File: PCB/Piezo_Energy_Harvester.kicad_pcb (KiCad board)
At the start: 2 copper layers, 26 x 20 mm, 9 parts, among them J1 Conn_01x01_Pin, J2 Conn_01x01_Pin, U1 LTC3588IMSE-1-PBF

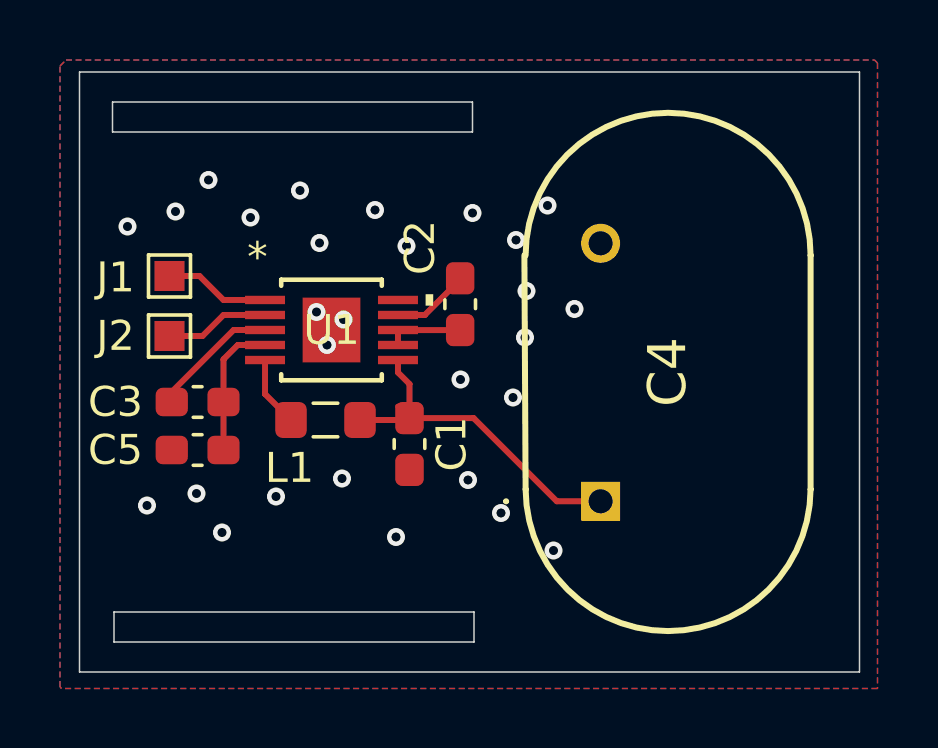
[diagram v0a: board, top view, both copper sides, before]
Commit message: changed coil footprint
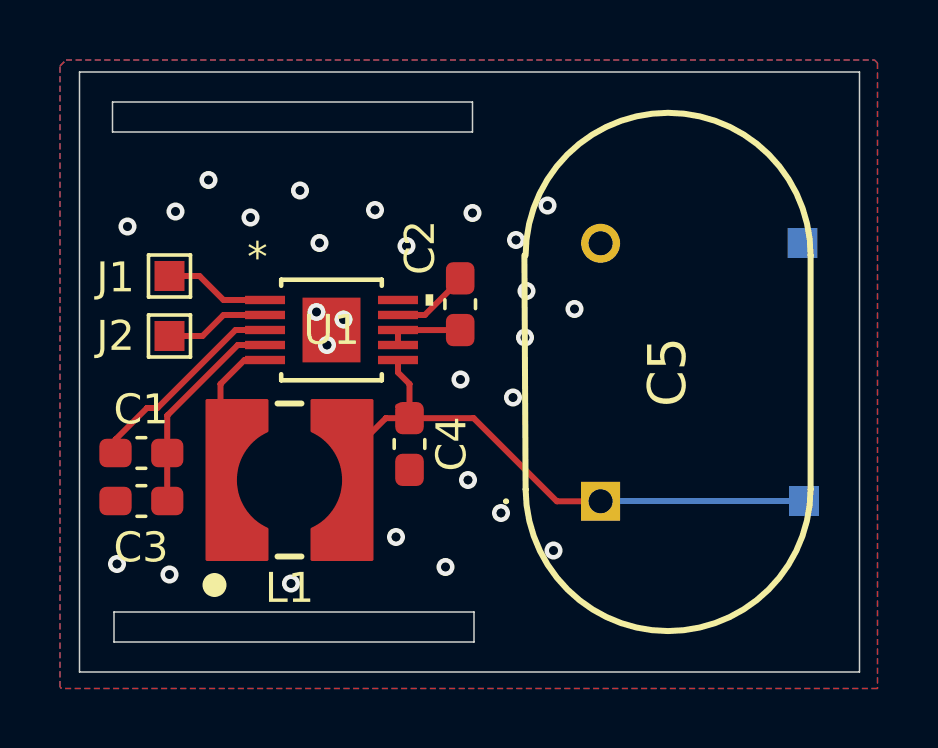
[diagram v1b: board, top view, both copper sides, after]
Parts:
- added ?: , , F.Cu at (172.9, 106.1)
- added ?: , , F.Cu at (172.9, 97.5)
- C3: renamed from C5; value 47u 25V -> 10u 25V
- L1: footprint Inductor_SMD:L_0805_2012Metric_Pad1.05x1.20mm_HandSolder -> Piezo_EH_footprints:WE-HEPC_5030
- moved C1 2.53 mm to (150.9, 104.5)
- moved C3 2.53 mm to (150.9, 106.1)
- moved L1 2.33 mm to (155.8, 105.4), turned to 90 degrees
- renumbered C3 to C1, C1 to C4, C4 to C5
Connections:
- U1 pad EPAD: GND -> (no net)
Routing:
- net +3.3V: track 11.8 -> 20.3 mm
- net Net-(U1-SW): track 2.36 -> 5.01 mm
- net Net-(U1-CAP): track 4.30 -> 6.95 mm
- net Net-(U1-VIN): track 4.60 -> 7.08 mm
- net GND: vias 28 -> 27

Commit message: C4 changed
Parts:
- C4: footprint Capacitor_SMD:C_0603_1608Metric_Pad1.08x0.95mm_HandSolder -> Capacitor_SMD:CP_Elec_5x5.4
- moved C1 5.02 mm to (152.6, 99.8)
- moved C3 5.02 mm to (152.6, 101.4)
- moved J1 3.56 mm to (150.2, 95.5)
- moved J2 3.56 mm to (150.2, 97.5)
- moved C2 3.15 mm to (161.5, 96.4)
- moved U1 3.15 mm to (157.2, 97.2)
- moved L1 2.90 mm to (152.9, 105.5), turned to 0 degrees
- moved C4 1.43 mm to (159.1, 105.5)
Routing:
- net +3.3V: track 20.3 -> 28.5 mm
- net Net-(U1-SW): track 5.01 -> 8.54 mm
- net Net-(U1-CAP): track 6.95 -> 4.53 mm
- net Net-(U1-VIN): track 7.08 -> 4.80 mm
- net Net-(J2-Pin_1): track 3.47 -> 5.12 mm
- net Net-(J1-Pin_1): track 3.51 -> 5.16 mm
- net GND: track 2.60 -> 4.25 mm, vias 27 -> 25

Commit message: Minor changes
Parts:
- moved C4 0.40 mm to (159.1, 105.0), turned to -90 degrees
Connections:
- C4 pad 1: GND -> +3.3V
- C4 pad 2: +3.3V -> GND
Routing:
- net +3.3V: track 28.5 -> 29.1 mm
- net GND: vias 25 -> 24
